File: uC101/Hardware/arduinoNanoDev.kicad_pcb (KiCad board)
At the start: 2 copper layers, 100 x 48 mm, 45 parts, among them J1 Serial / UART, J2 SPI Header, J3 I2C Header, J4 SAO_Conn, SW1 SW_Push, SW2 Rotary_Encoder_Switch, SW3 SW_Push

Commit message: more uC101 board changes
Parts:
- added J10: Conn_01x04, uC101:PinHole_1x04_P2.54mm_Vertical, F.Cu at (168.9, 67.3)
- added J5: Conn_01x10, uC101:PinHole_1x10_P2.54mm_Vertical, F.Cu at (171.4, 69.8)
- added J6: Conn_01x10, uC101:PinHole_1x10_P2.54mm_Vertical, F.Cu at (171.4, 72.4)
- added J7: Conn_01x10, uC101:PinHole_1x10_P2.54mm_Vertical, F.Cu at (171.4, 74.9)
- added J8: Conn_01x10, uC101:PinHole_1x10_P2.54mm_Vertical, F.Cu at (171.4, 67.3)
- added J9: Conn_01x04, uC101:PinHole_1x04_P2.54mm_Vertical, F.Cu at (196.8, 67.3)
- added REF**: Josh Details, VNA_Footprints:JoshDetails, B.Cu at (253.6, 68.2)
- added TP13: GND, TestPoint:TestPoint_THTPad_D1.5mm_Drill0.7mm, F.Cu at (200.0, 88.5)
- added TP14: GND, TestPoint:TestPoint_THTPad_D1.5mm_Drill0.7mm, F.Cu at (184.0, 82.0)
- J2: value SPI Header -> SPI
- J3: value I2C Header -> I2C
- moved J1 12.7 mm to (168.0, 59.5), turned to 90 degrees
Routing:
- net +5V: track 285.0 -> 297.0 mm
- net /TX: track 55.4 -> 45.9 mm
- net /RX: track 50.4 -> 47.8 mm
- net GND: track 4.15 -> 3.22 mm
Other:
- board text added: "Josh Johnson"
- board text added: "bit.ly/CBRhardware"
- board text added: "uC101"

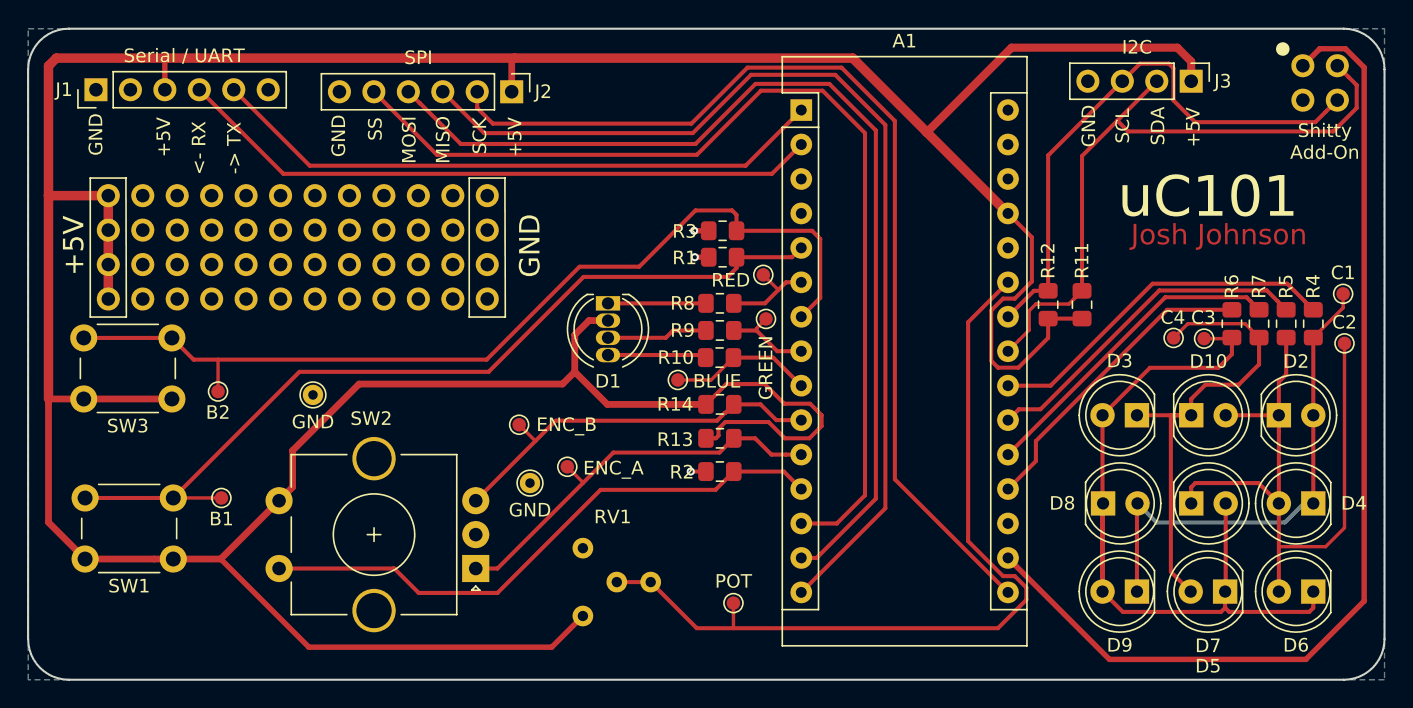
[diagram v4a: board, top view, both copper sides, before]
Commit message: more changes to arduinoNanoDev board
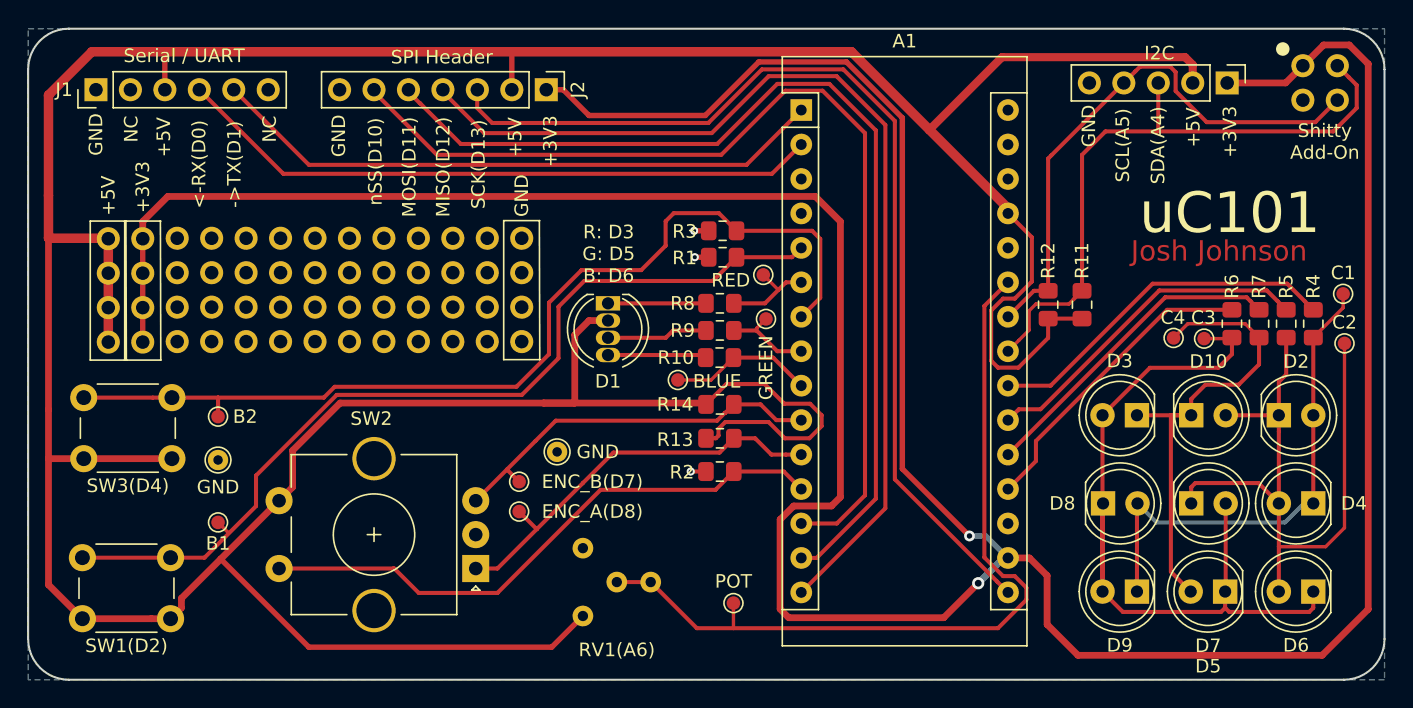
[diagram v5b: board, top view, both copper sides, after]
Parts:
- removed REF**: Josh Details, VNA_Footprints:JoshDetails
- added J11: Conn_01x04, uC101:PinHole_1x04_P2.54mm_Vertical, F.Cu at (171.4, 70.5)
- J2: value SPI -> SPI Header; footprint Connector_PinHeader_2.54mm:PinHeader_1x06_P2.54mm_Vertical -> Connector_PinHeader_2.54mm:PinHeader_1x07_P2.54mm_Vertical
- J3: footprint Connector_PinHeader_2.54mm:PinHeader_1x04_P2.54mm_Vertical -> Connector_PinHeader_2.54mm:PinHeader_1x05_P2.54mm_Vertical
- TP1: value ENC_B -> ENC_B(D7)
- TP3: value ENC_A -> ENC_A(D8)
- moved TP14 8.49 mm to (177.0, 86.8)
- moved TP3 4.85 mm to (199.2, 90.6)
- moved SW1(D2) 4.40 mm to (173.5, 98.5)
- moved SW3(D4) 4.40 mm to (173.6, 86.7)
- moved TP1 4.20 mm to (199.2, 88.4)
- moved J5 4.04 mm to (174.0, 73.0)
- moved J6 4.04 mm to (174.0, 75.5)
- moved J8 4.04 mm to (174.0, 70.5)
- moved J7 4.04 mm to (174.0, 78.1)
- moved J9 4.04 mm to (199.4, 70.5)
- moved J10 3.17 mm to (168.9, 70.5)
- moved TP13 3.05 mm to (202.0, 86.2)
- moved J3 2.65 mm to (251.4, 59.0)
- moved J2 2.55 mm to (201.2, 59.5)
- moved TP4 1.85 mm to (177.0, 83.6)
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- renumbered RV1 to RV1(A6), SW1 to SW1(D2), SW3 to SW3(D4)
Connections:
- A1 pad 13: /SS -> (no net)
- J2 pad 1: +5V -> +3V3
- J2 pad 2: /SCK -> +5V
- J2 pad 3: /MISO -> /SCK
- J2 pad 4: /MOSI -> /MISO
- J2 pad 5: /SS -> /MOSI
- J2 pad 6: GND -> /nSS
- J3 pad 1: +5V -> +3V3
- J3 pad 2: /SDA -> +5V
- J3 pad 3: /SCL -> /SDA
- J3 pad 4: GND -> /SCL
- J5 pad 1: Net-(J5-Pad1) -> (no net)
- J5 pad 10: Net-(J5-Pad10) -> (no net)
- J5 pad 2: Net-(J5-Pad2) -> (no net)
- J5 pad 3: Net-(J5-Pad3) -> (no net)
- J5 pad 4: Net-(J5-Pad4) -> (no net)
- J5 pad 5: Net-(J5-Pad5) -> (no net)
- J5 pad 6: Net-(J5-Pad6) -> (no net)
- J5 pad 7: Net-(J5-Pad7) -> (no net)
- J5 pad 8: Net-(J5-Pad8) -> (no net)
- J5 pad 9: Net-(J5-Pad9) -> (no net)
- J6 pad 1: Net-(J6-Pad1) -> (no net)
- J6 pad 10: Net-(J6-Pad10) -> (no net)
- J6 pad 2: Net-(J6-Pad2) -> (no net)
- J6 pad 3: Net-(J6-Pad3) -> (no net)
- J6 pad 4: Net-(J6-Pad4) -> (no net)
- J6 pad 5: Net-(J6-Pad5) -> (no net)
- J6 pad 6: Net-(J6-Pad6) -> (no net)
- J6 pad 7: Net-(J6-Pad7) -> (no net)
- J6 pad 8: Net-(J6-Pad8) -> (no net)
- J6 pad 9: Net-(J6-Pad9) -> (no net)
- J7 pad 1: Net-(J7-Pad1) -> (no net)
- J7 pad 10: Net-(J7-Pad10) -> (no net)
- J7 pad 2: Net-(J7-Pad2) -> (no net)
- J7 pad 3: Net-(J7-Pad3) -> (no net)
- J7 pad 4: Net-(J7-Pad4) -> (no net)
- J7 pad 5: Net-(J7-Pad5) -> (no net)
- J7 pad 6: Net-(J7-Pad6) -> (no net)
- J7 pad 7: Net-(J7-Pad7) -> (no net)
- J7 pad 8: Net-(J7-Pad8) -> (no net)
- J7 pad 9: Net-(J7-Pad9) -> (no net)
- J8 pad 1: Net-(J8-Pad1) -> (no net)
- J8 pad 10: Net-(J8-Pad10) -> (no net)
- J8 pad 2: Net-(J8-Pad2) -> (no net)
- J8 pad 3: Net-(J8-Pad3) -> (no net)
- J8 pad 4: Net-(J8-Pad4) -> (no net)
- J8 pad 5: Net-(J8-Pad5) -> (no net)
- J8 pad 6: Net-(J8-Pad6) -> (no net)
- J8 pad 7: Net-(J8-Pad7) -> (no net)
- J8 pad 8: Net-(J8-Pad8) -> (no net)
- J8 pad 9: Net-(J8-Pad9) -> (no net)
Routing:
- net +3V3: track 76.1 -> 265.0 mm, vias 0 -> 2
- net /SS: track 73.7 -> 0.00 mm
- net (no net): track 0.00 -> 73.7 mm
- net +5V: track 297.0 -> 308.8 mm
- net /BUTTON_1: track 64.5 -> 67.2 mm
- net /BUTTON_2: track 69.7 -> 71.7 mm
- net /SDA: track 48.3 -> 47.2 mm
- net /POT: track 61.2 -> 60.2 mm
- net /SCL: track 41.7 -> 40.8 mm
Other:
- board text added: "+3V3"
- board text added: "->TX(D1)"
- board text added: "<-RX(D0)"
- board text added: "MISO(D12)"
- board text added: "MOSI(D11)"
- board text added: "NC"
- board text added: "R: D3 G: D5 B: D6"
- board text added: "SCK(D13)"
- board text added: "SCL(A5)"
- board text added: "SDA(A4)"
- board text added: "nSS(D10)"
- board text removed: "-> TX"
- board text removed: "<- RX"
- board text removed: "MISO"
- board text removed: "MOSI"
- board text removed: "SCK"
- board text removed: "SCL"
- board text removed: "SDA"
- board text removed: "SS"

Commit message: More board updates + updated readme
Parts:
- added TP15: ENC_SW(D9), TestPoint:TestPoint_Pad_D1.0mm, F.Cu at (181.5, 100.5)
- J3: value I2C -> I2C Header
- renumbered SW3(D4) to SW2(D4), SW2 to SW3
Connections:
- A1 pad 13: (no net) -> /nSS
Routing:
- net /nSS: track 0.00 -> 73.7 mm
- net (no net): track 73.7 -> 0.00 mm
- net +3V3: track 265.0 -> 203.0 mm, vias 2 -> 1
- net /ENCODER_SW: track 43.7 -> 49.4 mm
- net +5V: track 308.8 -> 311.7 mm

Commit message: More board changes + updated RouteMe with latest netlist
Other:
- board text added: "ATmega328p PD1(TXD) PD0(RXD) PD2(INT0) PD3(INT1) PD4 PD5 PD6 PD7 PB0 PB1 PB2(nSS) PB3(MOSI) PB4(MISO) PB5(SCK) PC0 PC1 PC2 PC3 PC4(SDA) PC5(SCL) ADC6 ADC7"
- board text added: "Arduino 1(TX) 0(RX) D2 D3 D4 D5 D6 D7 D8 D9 D10 D11 D12 D13 A0 A1 A2 A3 A4 A5 A6 A7"

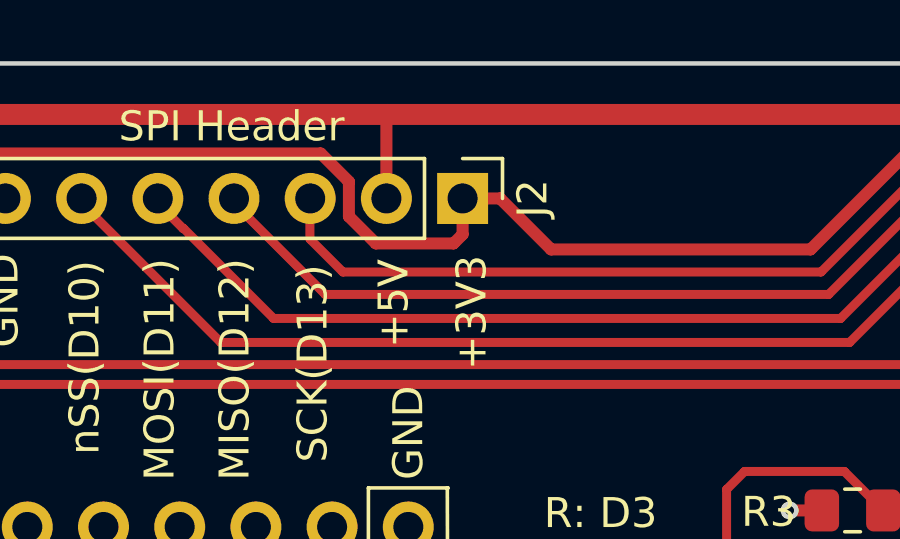
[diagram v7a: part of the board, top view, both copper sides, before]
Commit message: Panellisation and sending off of gerbers
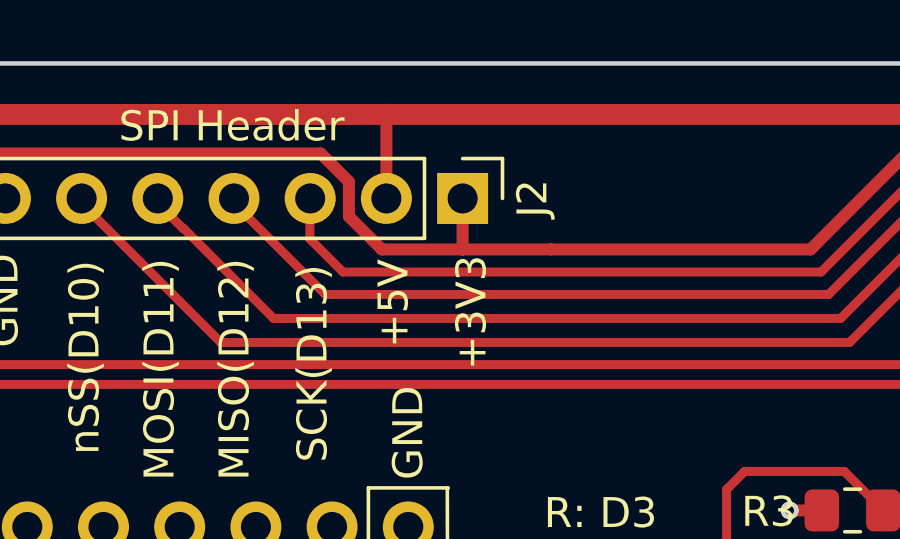
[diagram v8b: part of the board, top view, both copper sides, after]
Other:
- board text removed: "bit.ly/CBRhardware"
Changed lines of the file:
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@@
   (general
     (thickness 1.6)
-    (drawings 37)
-    (tracks 372)
+    (drawings 36)
+    (tracks 370)
     (zones 0)
     (modules 55)
@@
   (page A4)
   (layers
-    (0 F.Cu signal hide)
+    (0 F.Cu signal)
     (31 B.Cu signal)
     (32 B.Adhes user)
@@
     (visible_elements 7FFFFFFF)
     (pcbplotparams
-      (layerselection 0x010fc_ffffffff)
-      (usegerberextensions false)
+      (layerselection 0x010f8_ffffffff)
+      (usegerberextensions true)
       (usegerberattributes false)
       (usegerberadvancedattributes false)
@@
       (outputformat 1)
       (mirror false)
-      (drillshape 1)
+      (drillshape 0)
       (scaleselection 1)
-      (outputdirectory ""))
+      (outputdirectory "gerbers/"))
   )
   (net 0 "")
@@
   (gr_text +3V3 (at 171.45 66.675 90) (layer F.SilkS)
     (effects (font (size 1 1) (thickness 0.2)))
-  )
-  (gr_text bit.ly/CBRhardware (at 251 71.6) (layer B.SilkS)
-    (effects (font (size 1 1) (thickness 0.15)) (justify mirror))
   )
   (gr_text GND (at 199.39 67.31 90) (layer F.SilkS)
@@
   (segment (start 232.4 92.4) (end 233.6 92.4) (width 0.4) (layer B.Cu) (net 30))
   (segment (start 233.6 92.4) (end 235.22 94.02) (width 0.4) (layer B.Cu) (net 30))
-  (segment (start 204.15 61.2) (end 202.45 59.5) (width 0.4) (layer F.Cu) (net 30))
   (segment (start 227.45001 87.45001) (end 227.45001 61.577549) (width 0.4) (layer F.Cu) (net 30))
   (segment (start 232.4 92.4) (end 227.45001 87.45001) (width 0.4) (layer F.Cu) (net 30))
   (segment (start 227.45001 61.577549) (end 223.322472 57.450011) (width 0.4) (layer F.Cu) (net 30))
-  (segment (start 202.45 59.5) (end 201.2 59.5) (width 0.4) (layer F.Cu) (net 30))
   (segment (start 223.322472 57.450011) (end 216.549989 57.450011) (width 0.4) (layer F.Cu) (net 30))
   (segment (start 216.549989 57.450011) (end 212.8 61.2) (width 0.4) (layer F.Cu) (net 30))
   (segment (start 212.8 61.2) (end 204.15 61.2) (width 0.4) (layer F.Cu) (net 30))
-  (segment (start 200.9 61) (end 201.2 60.7) (width 0.4) (layer F.Cu) (net 30))
-  (segment (start 198.309998 61) (end 200.9 61) (width 0.4) (layer F.Cu) (net 30))
-  (segment (start 201.2 60.7) (end 201.2 59.5) (width 0.4) (layer F.Cu) (net 30))
+  (segment (start 197.409999 60.100001) (end 198.509998 61.2) (width 0.4) (layer F.Cu) (net 30))
   (segment (start 197.409999 58.939997) (end 197.409999 60.100001) (width 0.4) (layer F.Cu) (net 30))
-  (segment (start 197.409999 60.100001) (end 198.309998 61) (width 0.4) (layer F.Cu) (net 30))
-  (segment (start 175 58) (end 196.470002 58) (width 0.4) (layer F.Cu) (net 30))
   (segment (start 174.328548 58.671452) (end 175 58) (width 0.4) (layer F.Cu) (net 30))
+  (segment (start 196.470002 58) (end 197.409999 58.939997) (width 0.4) (layer F.Cu) (net 30))
   (segment (start 174.328548 58.898546) (end 174.328548 58.671452) (width 0.4) (layer F.Cu) (net 30))
   (segment (start 171.45 69.407096) (end 174.328548 66.528548) (width 0.4) (layer F.Cu) (net 30))
+  (segment (start 175 58) (end 196.470002 58) (width 0.4) (layer F.Cu) (net 30))
   (segment (start 171.45 70.485) (end 171.45 69.407096) (width 0.4) (layer F.Cu) (net 30))
-  (segment (start 196.470002 58) (end 197.409999 58.939997) (width 0.4) (layer F.Cu) (net 30))
+  (segment (start 174.328548 66.528548) (end 174.328548 60.101454) (width 0.4) (layer F.Cu) (net 30))
   (segment (start 174.328548 60.101454) (end 174.330001 60.100001) (width 0.4) (layer F.Cu) (net 30))
-  (segment (start 174.328548 66.528548) (end 174.328548 60.101454) (width 0.4) (layer F.Cu) (net 30))
   (segment (start 174.330001 60.100001) (end 174.330001 58.899999) (width 0.4) (layer F.Cu) (net 30))
   (segment (start 174.330001 58.899999) (end 174.328548 58.898546) (width 0.4) (layer F.Cu) (net 30))
+  (segment (start 201.2 61.2) (end 201.2 59.5) (width 0.4) (layer F.Cu) (net 30))
+  (segment (start 198.509998 61.2) (end 201.2 61.2) (width 0.4) (layer F.Cu) (net 30))
+  (segment (start 201.2 61.2) (end 204.15 61.2) (width 0.4) (layer F.Cu) (net 30))
   (segment (start 222.62 91.48) (end 224.7 89.4) (width 0.3) (layer F.Cu) (net 31))
   (segment (start 193.14 64.3) (end 188.49 59.65) (width 0.3) (layer F.Cu) (net 31))
